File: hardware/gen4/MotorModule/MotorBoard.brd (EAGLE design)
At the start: 35.4 x 61.7 mm, 66 parts, among them IC1 XMEGA16A4A, IC2 3.3V REG, M1O1 TEST_PT, M1O2 TEST_PT, M1O3 TEST_PT

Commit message: more fixes
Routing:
- net GND: track 79.9 -> 81.9 mm
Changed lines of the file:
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@@
 </class>
 </classes>
-<designrules name="SparkFun *">
-<description language="en">&lt;b&gt;Design Rules for Advanced Circuits (4pcb.com)&lt;/b&gt;
+<designrules name="eC_2Layer_PClass6_BaseCopperO18_eCDefault">
+<description language="de">
 &lt;p&gt;
-Min trace width, spacing, drill size and dimension clearance for Advanced Circuits; avoids surcharges for extra small spacing/trace widths
+&lt;b&gt;Eurocircuits-EAGLE design rules&lt;/b&gt;&lt;br&gt;
+&lt;br&gt;
+Setup for &lt;b&gt;2-layer PatternClass6 BaseCopperO18 eCDefault&lt;/b&gt;
 &lt;p&gt;
-2-Layer</description>
+ The option &lt;b&gt;Sizes-Minimum Drill&lt;/b&gt; is set to 0.35mm. This minimum drill endsize can be set lower if needed. Values below 0.25mm will result in a higher DrillClassification. For details see the Eurocircuits Classification overview.
+&lt;p&gt;
+&lt;u&gt;Extra Notes:&lt;/u&gt;&lt;br&gt;
+- The option &lt;b&gt;Distance-Copper/Dimension&lt;/b&gt; is set to 0.25mm, the default for boards with a routed boardoutline. If you require Vcut on your board this parameter should be set to 0.45mm.&lt;br&gt;
+- The option &lt;b&gt;Supply-Generate thermals for vias&lt;/b&gt; is on by default but may be changed if required.&lt;br&gt;
+- The option &lt;b&gt;Mask-Stop&lt;/b&gt; is set to 0mm oversize which is the preffered value.&lt;br&gt;
+- The option &lt;b&gt;Mask-Cream&lt;/b&gt; is set to 0mm oversize by default, but may be changed if required&lt;br&gt;
+- The option &lt;b&gt;Mask-Limit&lt;/b&gt; is set to 0.45mm, resulting in covered or tented via holes for vias of 0.45mm and smaller. The option may be changed if required.&lt;br&gt;
+- The options &lt;b&gt;Shapes&lt;/b&gt; and &lt;b&gt;Misc&lt;/b&gt; are not relevant. Values for &lt;b&gt;Shapes-Smds-Roundness&lt;/b&gt; are not critical and can be set as you require.
+&lt;p&gt;
+&lt;p&gt;
+You can set higher minimum values if you wish, setting lower minimum values is &lt;u&gt;not advisable&lt;/u&gt;.&lt;br&gt;
+If you need lower minimum values, please use a different Eurocircuits-EAGLE design rule file. For details see the Eurocircuits-EAGLE dru overview table.
+&lt;p&gt;
+Your Eurocircuits Team
+</description>
+<description language="en">
+&lt;p&gt;
+&lt;b&gt;Eurocircuits-EAGLE design rules&lt;/b&gt;&lt;br&gt;
+&lt;br&gt;
+Setup for &lt;b&gt;2-layer PatternClass6 BaseCopperO18 eCDefault&lt;/b&gt;
+&lt;p&gt;
+ The option &lt;b&gt;Sizes-Minimum Drill&lt;/b&gt; is set to 0.35mm. This minimum drill endsize can be set lower if needed. Values below 0.25mm will result in a higher DrillClassification. For details see the Eurocircuits Classification overview.
+&lt;p&gt;
+&lt;u&gt;Extra Notes:&lt;/u&gt;&lt;br&gt;
+- The option &lt;b&gt;Distance-Copper/Dimension&lt;/b&gt; is set to 0.25mm, the default for boards with a routed boardoutline. If you require Vcut on your board this parameter should be set to 0.45mm.&lt;br&gt;
+- The option &lt;b&gt;Supply-Generate thermals for vias&lt;/b&gt; is on by default but may be changed if required.&lt;br&gt;
+- The option &lt;b&gt;Mask-Stop&lt;/b&gt; is set to 0mm oversize which is the preffered value.&lt;br&gt;
+- The option &lt;b&gt;Mask-Cream&lt;/b&gt; is set to 0mm oversize by default, but may be changed if required&lt;br&gt;
+- The option &lt;b&gt;Mask-Limit&lt;/b&gt; is set to 0.45mm, resulting in covered or tented via holes for vias of 0.45mm and smaller. The option may be changed if required.&lt;br&gt;
+- The options &lt;b&gt;Shapes&lt;/b&gt; and &lt;b&gt;Misc&lt;/b&gt; are not relevant. Values for &lt;b&gt;Shapes-Smds-Roundness&lt;/b&gt; are not critical and can be set as you require.
+&lt;p&gt;
+&lt;p&gt;
+You can set higher minimum values if you wish, setting lower minimum values is &lt;u&gt;not advisable&lt;/u&gt;.&lt;br&gt;
+If you need lower minimum values, please use a different Eurocircuits-EAGLE design rule file. For details see the Eurocircuits-EAGLE dru overview table.
+&lt;p&gt;
+Your Eurocircuits Team
+</description>
 <param name="layerSetup" value="(1*16)"/>
 <param name="mtCopper" value="0.018mm 0.035mm 0.035mm 0.035mm 0.035mm 0.035mm 0.035mm 0.035mm 0.035mm 0.035mm 0.035mm 0.035mm 0.035mm 0.035mm 0.035mm 0.018mm"/>
-<param name="mtIsolate" value="1.5mm 0.15mm 0.2mm 0.15mm 0.2mm 0.15mm 0.2mm 0.15mm 0.2mm 0.15mm 0.2mm 0.15mm 0.2mm 0.15mm 0.2mm"/>
+<param name="mtIsolate" value="1.55mm 0.71mm 0.36mm 0.2mm 0.2mm 0.2mm 0.2mm 0.15mm 0.2mm 0.15mm 0.2mm 0.15mm 0.2mm 0.15mm 0.2mm"/>
 <param name="mdWireWire" value="0.15mm"/>
 <param name="mdWirePad" value="0.15mm"/>
@@
 <param name="mdPadVia" value="0.15mm"/>
 <param name="mdViaVia" value="0.15mm"/>
-<param name="mdSmdPad" value="0.15mm"/>
-<param name="mdSmdVia" value="0.15mm"/>
-<param name="mdSmdSmd" value="0.15mm"/>
-<param name="mdViaViaSameLayer" value="8mil"/>
+<param name="mdSmdPad" value="0mil"/>
+<param name="mdSmdVia" value="0mil"/>
+<param name="mdSmdSmd" value="0mil"/>
+<param name="mdViaViaSameLayer" value="0.2mm"/>
 <param name="mnLayersViaInSmd" value="2"/>
 <param name="mdCopperDimension" value="0.25mm"/>
-<param name="mdDrill" value="0.25mm"/>
+<param name="mdDrill" value="0.35mm"/>
 <param name="mdSmdStop" value="0mil"/>
 <param name="msWidth" value="0.15mm"/>
-<param name="msDrill" value="0.25mm"/>
-<param name="msMicroVia" value="9.99mm"/>
+<param name="msDrill" value="0.35mm"/>
+<param name="msMicroVia" value="25mm"/>
 <param name="msBlindViaRatio" value="0.5"/>
 <param name="rvPadTop" value="0.25"/>
@@
 <param name="rvViaOuter" value="0.25"/>
 <param name="rvViaInner" value="0.25"/>
-<param name="rvMicroViaOuter" value="0.25"/>
-<param name="rvMicroViaInner" value="0.25"/>
-<param name="rlMinPadTop" value="10mil"/>
-<param name="rlMaxPadTop" value="20mil"/>
-<param name="rlMinPadInner" value="10mil"/>
-<param name="rlMaxPadInner" value="20mil"/>
-<param name="rlMinPadBottom" value="10mil"/>
-<param name="rlMaxPadBottom" value="20mil"/>
-<param name="rlMinViaOuter" value="8mil"/>
-<param name="rlMaxViaOuter" value="20mil"/>
-<param name="rlMinViaInner" value="8mil"/>
-<param name="rlMaxViaInner" value="20mil"/>
-<param name="rlMinMicroViaOuter" value="4mil"/>
-<param name="rlMaxMicroViaOuter" value="20mil"/>
-<param name="rlMinMicroViaInner" value="4mil"/>
-<param name="rlMaxMicroViaInner" value="20mil"/>
+<param name="rvMicroViaOuter" value="0"/>
+<param name="rvMicroViaInner" value="0"/>
+<param name="rlMinPadTop" value="0.175mm"/>
+<param name="rlMaxPadTop" value="2.5mm"/>
+<param name="rlMinPadInner" value="0.175mm"/>
+<param name="rlMaxPadInner" value="2.5mm"/>
+<param name="rlMinPadBottom" value="0.175mm"/>
+<param name="rlMaxPadBottom" value="2.5mm"/>
+<param name="rlMinViaOuter" value="0.125mm"/>
+<param name="rlMaxViaOuter" value="2.5mm"/>
+<param name="rlMinViaInner" value="0.125mm"/>
+<param name="rlMaxViaInner" value="2.5mm"/>
+<param name="rlMinMicroViaOuter" value="2.5mm"/>
+<param name="rlMaxMicroViaOuter" value="25mm"/>
+<param name="rlMinMicroViaInner" value="2.5mm"/>
+<param name="rlMaxMicroViaInner" value="25mm"/>
 <param name="psTop" value="-1"/>
 <param name="psBottom" value="-1"/>
@@
 <param name="psElongationLong" value="100"/>
 <param name="psElongationOffset" value="100"/>
-<param name="mvStopFrame" value="1"/>
+<param name="mvStopFrame" value="0"/>
 <param name="mvCreamFrame" value="0"/>
-<param name="mlMinStopFrame" value="4mil"/>
-<param name="mlMaxStopFrame" value="4mil"/>
+<param name="mlMinStopFrame" value="0mil"/>
+<param name="mlMaxStopFrame" value="0mil"/>
 <param name="mlMinCreamFrame" value="0mil"/>
 <param name="mlMaxCreamFrame" value="0mil"/>
-<param name="mlViaStopLimit" value="0mil"/>
+<param name="mlViaStopLimit" value="0.45mm"/>
 <param name="srRoundness" value="0"/>
 <param name="srMinRoundness" value="0mil"/>
 <param name="srMaxRoundness" value="0mil"/>
-<param name="slThermalIsolate" value="10mil"/>
-<param name="slThermalsForVias" value="0"/>
+<param name="slThermalIsolate" value="0.2mm"/>
+<param name="slThermalsForVias" value="1"/>
 <param name="dpMaxLengthDifference" value="10mm"/>
 <param name="dpGapFactor" value="2.5"/>
@@
 <contactref element="C46" pad="2"/>
 <contactref element="C45" pad="2"/>
-<polygon width="0.4064" layer="1">
+<polygon width="0.4064" layer="1" isolate="0.254">
 <vertex x="35.1753125" y="44.47625"/>
 <vertex x="0.0475" y="44.635"/>
@@
 <contactref element="U$1" pad="26"/>
 <contactref element="U$1" pad="P$3"/>
-<polygon width="0.4064" layer="16">
+<polygon width="0.4064" layer="16" isolate="0.254">
 <vertex x="0.0475" y="44.635"/>
 <vertex x="-0.0478125" y="-15.9209375"/>
@@
 <wire x1="30.023528125" y1="2.4735875" x2="29.901475" y2="2.351534375" width="0.254" layer="1"/>
 <contactref element="U$2" pad="2"/>
+<wire x1="28.09875" y1="1.42875" x2="29.901475" y2="2.351534375" width="0.254" layer="1"/>
 </signal>
 <signal name="MOSI">
@@
 </signal>
 </signals>
-<errors>
-</errors>
 </board>
 </drawing>

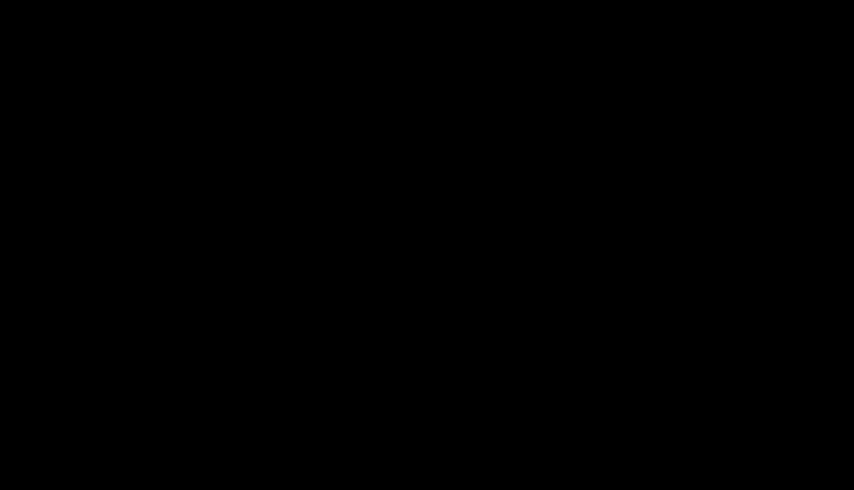
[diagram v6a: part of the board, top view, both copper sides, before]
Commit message: deleted unneccessary signals
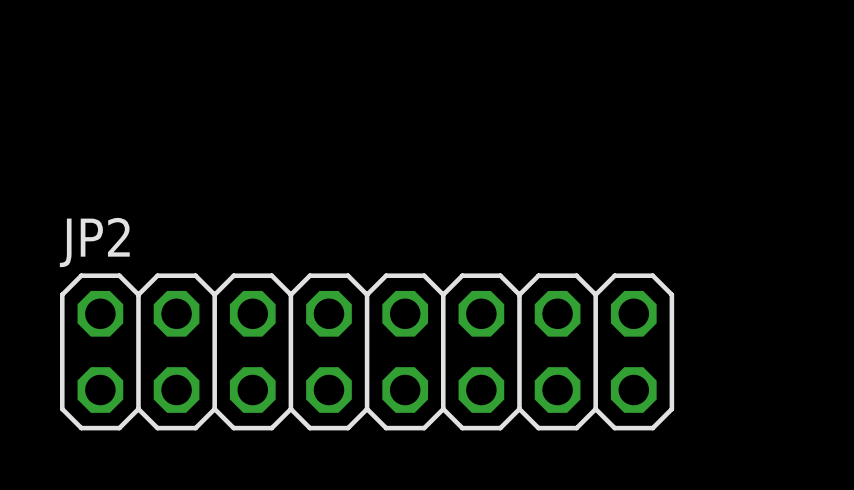
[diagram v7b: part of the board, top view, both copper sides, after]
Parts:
- added JP2: (no value), pinhead:2X08
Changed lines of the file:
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@@
 <element name="JP1" library="pinhead" package="2X05" value="DEBUG" x="29.36875" y="-3.65125" rot="R90"/>
 <element name="U$2" library="gen3" package="0805" value="INDUCTOR" x="4.392165625" y="-11.6639" rot="MR0"/>
+<element name="JP2" library="pinhead" package="2X08" value="" x="-79.164665625" y="-22.312346875"/>
 </elements>
 <signals>
